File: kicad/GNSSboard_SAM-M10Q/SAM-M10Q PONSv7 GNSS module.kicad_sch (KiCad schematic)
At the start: 8 parts, among them J1 2005280040, U2 SAM-M10Q-00B

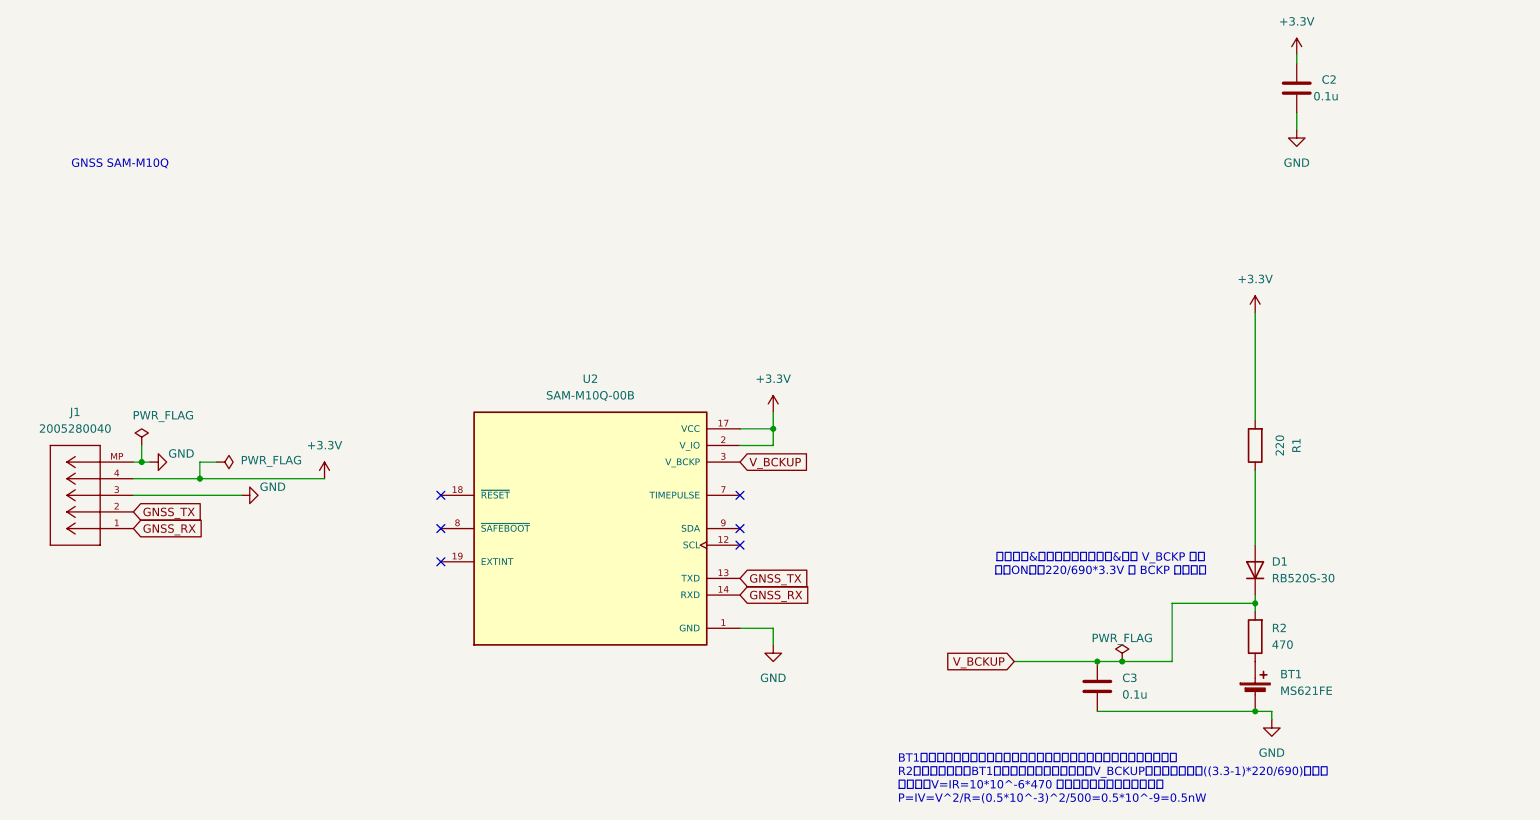
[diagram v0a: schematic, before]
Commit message: 0.961 KiCad更新 wav更新
wav雑音除去
kicad更新（スイッチ背面、DocへのQRコード更新）
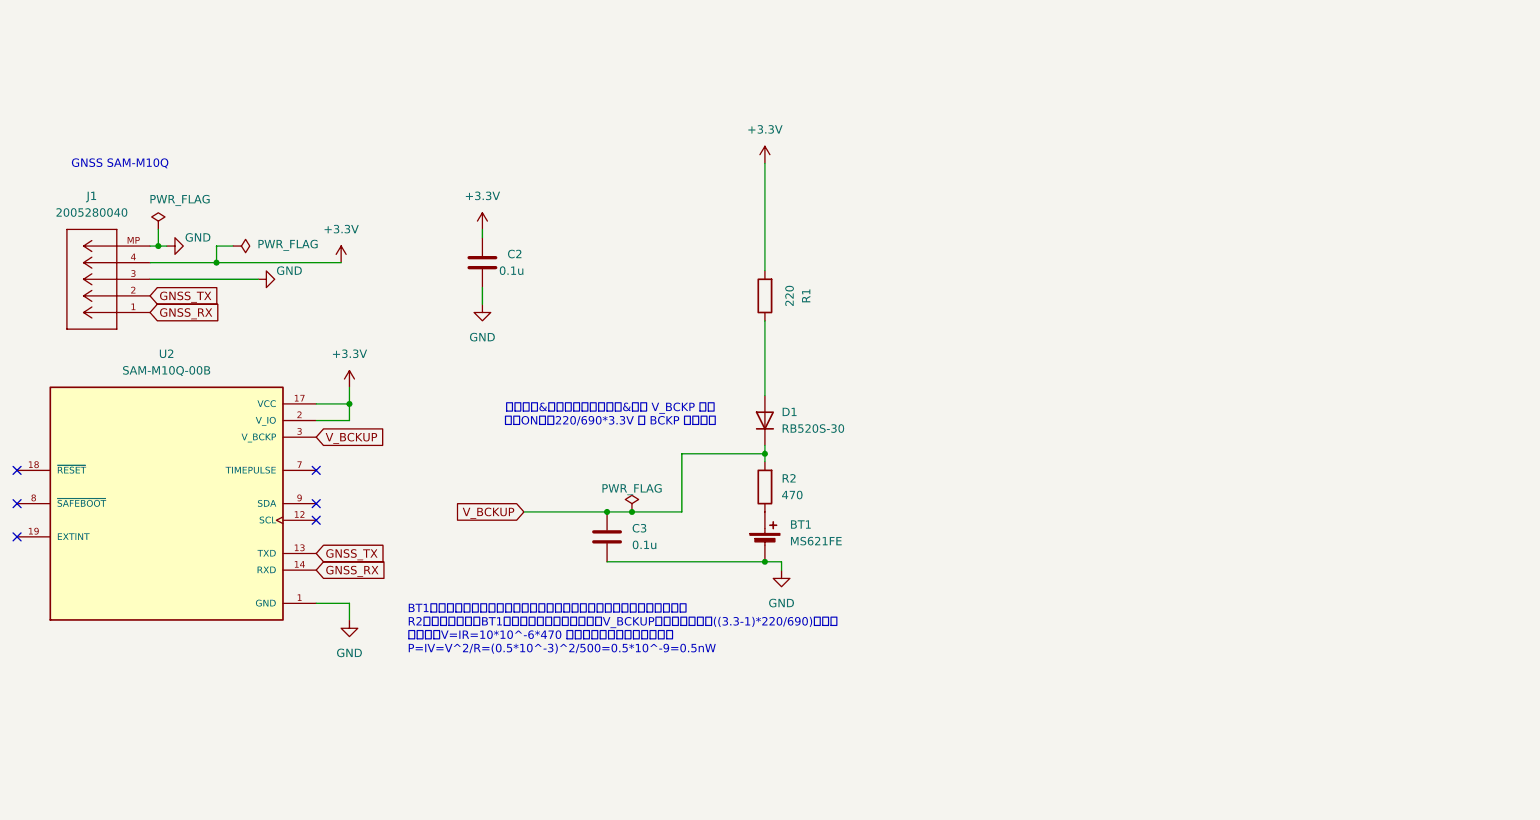
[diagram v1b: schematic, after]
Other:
- moved on the sheet: BT1, C2, C3, D1, J1, R1, R2, U2
